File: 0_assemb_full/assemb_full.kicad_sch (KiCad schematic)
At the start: 12 parts, among them J1 Conn_01x02, J2 Conn_02x06, J3 AudioJack3, J4 SPIConn_01x03, J5 SPIConn_01x03, J6 SPIConn_01x03, J7 SPIConn_01x03, J8 SPIConn_01x03, U1 LM2902, U2 LM1117-3.3

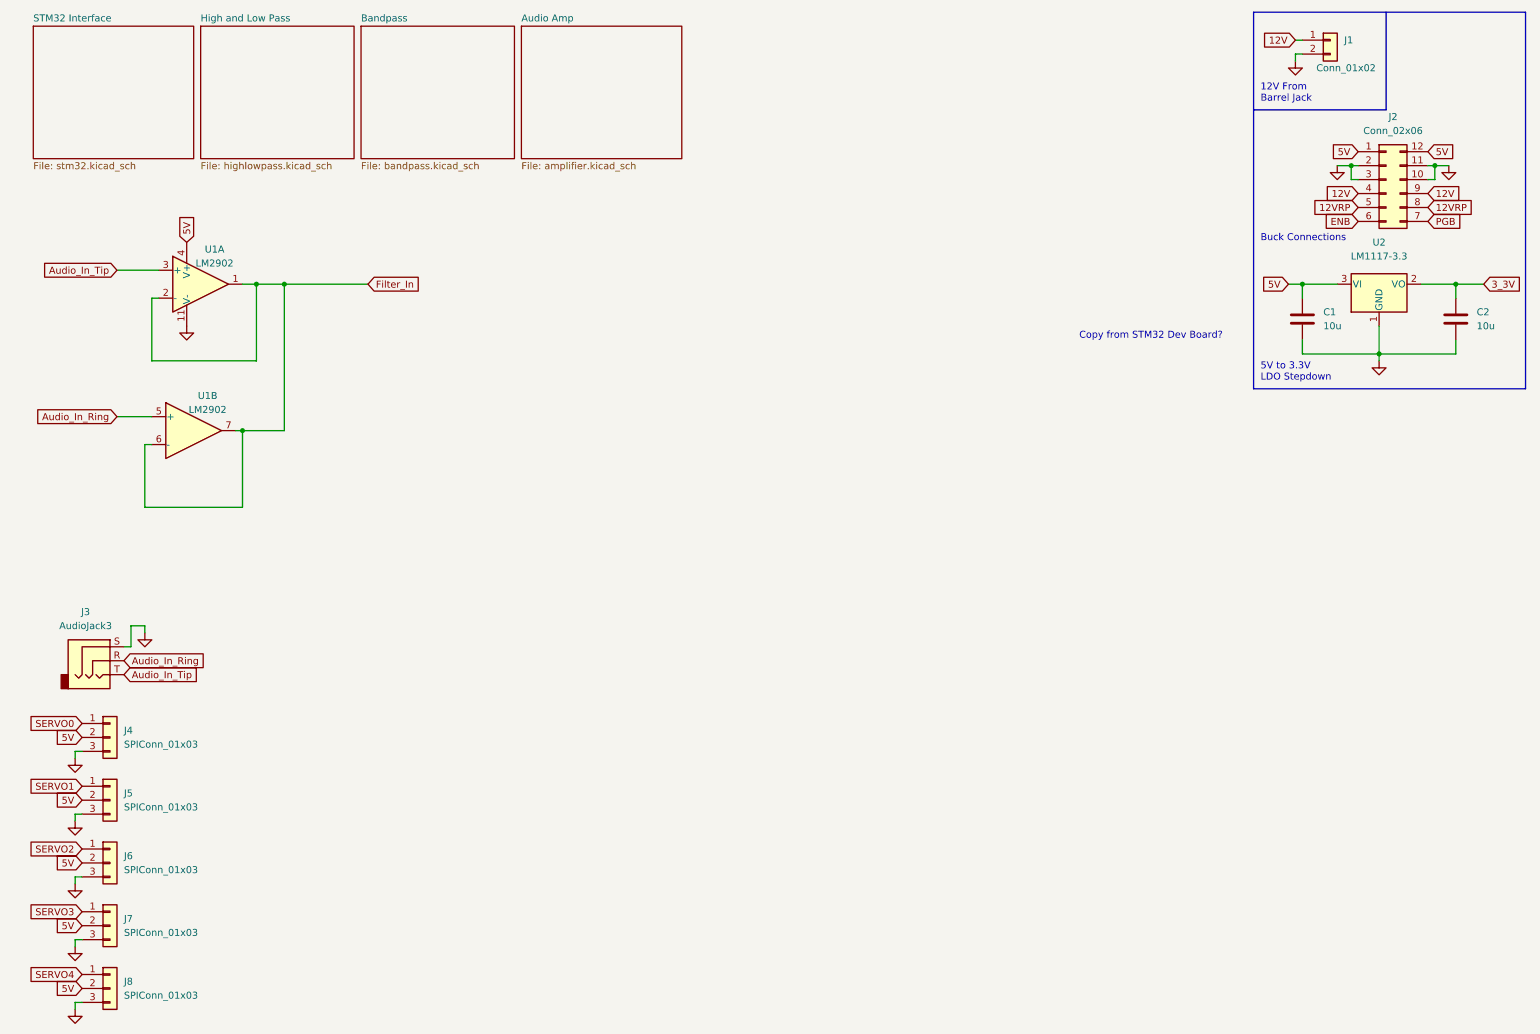
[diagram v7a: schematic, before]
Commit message: A lot of work done on the STM32 PCB layout.
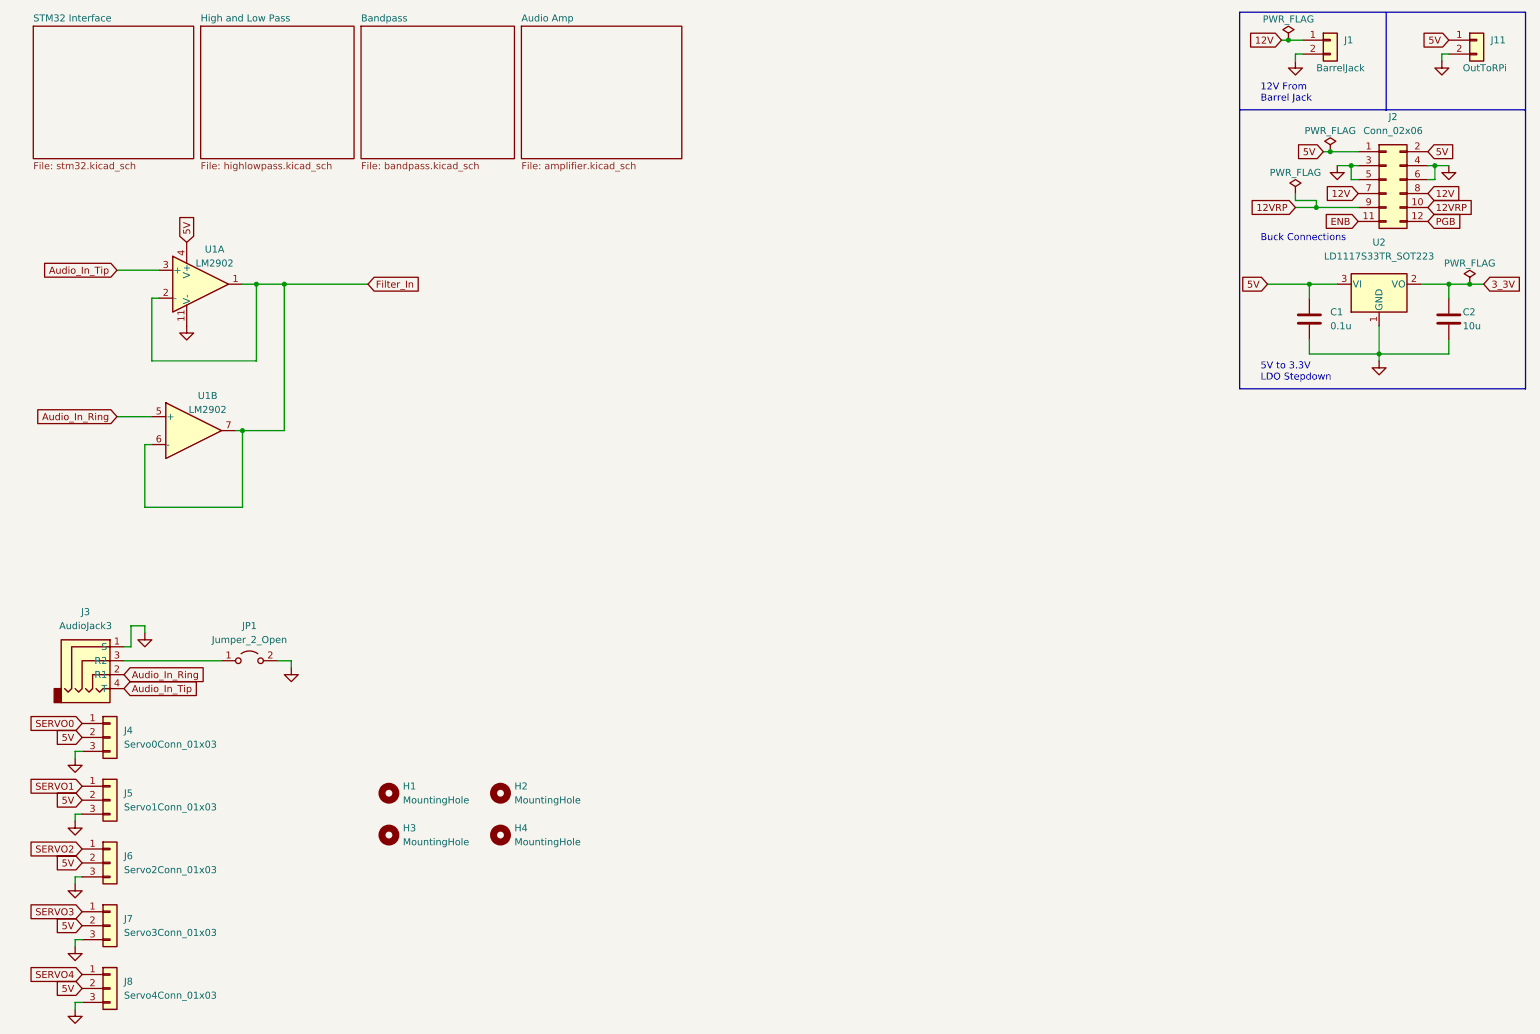
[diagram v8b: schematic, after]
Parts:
- removed U2: LM1117-3.3, symbol Regulator_Linear:LM1117-3.3
- added H1, H2, H3, H4: MountingHole, MountingHole:MountingHole_6.4mm_M6, symbol Mechanical:MountingHole
- added J11: OutToRPi, Connector_PinHeader_2.54mm:PinHeader_1x02_P2.54mm_Vertical, symbol Connector_Generic:Conn_01x02
- added JP1: Jumper_2_Open, Jumper:SolderJumper-2_P1.3mm_Open_Pad1.0x1.5mm, symbol Jumper:Jumper_2_Open
- added U2: LD1117S33TR_SOT223, Package_TO_SOT_SMD:SOT-223-3_TabPin2, symbol Regulator_Linear:LD1117S33TR_SOT223
- C1: value 10u -> 0.1u; footprint (none) -> Capacitor_SMD:C_0805_2012Metric_Pad1.18x1.45mm_HandSolder
- C2: footprint (none) -> Capacitor_THT:CP_Radial_D5.0mm_P2.00mm
- J1: value Conn_01x02 -> BarrelJack
- J2: footprint (none) -> Connector_PinSocket_2.54mm:PinSocket_2x06_P2.54mm_Vertical; symbol Connector_Generic:Conn_02x06_Counter_Clockwise -> Connector_Generic:Conn_02x06_Odd_Even
- J3: footprint (none) -> Connector_PinSocket_2.54mm:PinSocket_1x04_P2.54mm_Vertical; symbol Connector:AudioJack3 -> Connector:AudioJack4
- J4: value SPIConn_01x03 -> Servo0Conn_01x03; footprint (none) -> Connector_PinSocket_2.54mm:PinSocket_1x03_P2.54mm_Vertical
- J5: value SPIConn_01x03 -> Servo1Conn_01x03; footprint (none) -> Connector_PinSocket_2.54mm:PinSocket_1x03_P2.54mm_Vertical
- J6: value SPIConn_01x03 -> Servo2Conn_01x03; footprint (none) -> Connector_PinSocket_2.54mm:PinSocket_1x03_P2.54mm_Vertical
- J7: value SPIConn_01x03 -> Servo3Conn_01x03; footprint (none) -> Connector_PinSocket_2.54mm:PinSocket_1x03_P2.54mm_Vertical
- J8: value SPIConn_01x03 -> Servo4Conn_01x03; footprint (none) -> Connector_PinSocket_2.54mm:PinSocket_1x03_P2.54mm_Vertical
- U1: footprint (none) -> Package_DIP:DIP-14_W7.62mm
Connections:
- net 12V: now also J2.7 (Pin_7), J2.8 (Pin_8); no longer J2.4 (Pin_4), J2.9 (Pin_9)
- net 12VRP: now also J2.10 (Pin_10), J2.9 (Pin_9); no longer J2.5 (Pin_5), J2.8 (Pin_8)
- net 3_3V: now also U2.2 (VO)
- net 5V: now also J2.2 (Pin_2), J11.1 (Pin_1), U2.3 (VI); no longer J2.12 (Pin_12)
- net Audio_In_Ring: now also J3.2 (R1); no longer J3.R
- net Audio_In_Tip: now also J3.4 (T); no longer J3.T
- net ENB: now also J2.11 (Pin_11); no longer J2.6 (Pin_6)
- net GND: now also J2.4 (Pin_4), J2.5 (Pin_5), J2.6 (Pin_6), J3.1 (S), J11.2 (Pin_2), JP1.2 (B), U2.1 (GND); no longer J2.10 (Pin_10), J2.11 (Pin_11), J2.2 (Pin_2), J3.S
- net PGB: now also J2.12 (Pin_12); no longer J2.7 (Pin_7)
- new net: J3.3 (R2), JP1.1 (A)
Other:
- note removed: "Copy from STM32 Dev Board?"
- moved on the sheet: C2
